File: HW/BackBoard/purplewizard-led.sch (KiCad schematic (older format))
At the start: 30 parts, among them U6 IS31FL3736

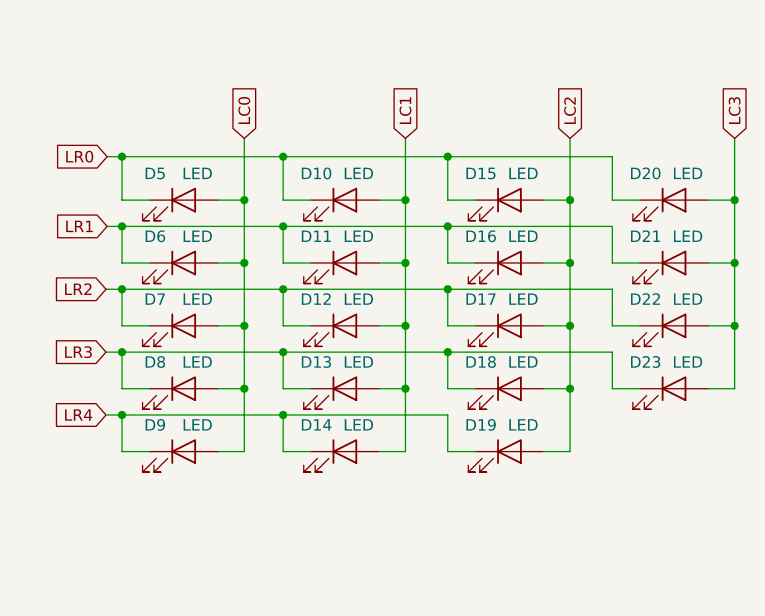
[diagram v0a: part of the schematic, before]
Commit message: Backboard - Move LCD connector over .3mm for better fitment of ribbon - Fix audio chip missing exposed pad bond to ground - Remove nRESET signal from JTAG - Reuse freed pin above to run an interrupt line from the keyboard controller to the MCU to enable interrupt driven keyboard input.  Protos will have a hack-n-jump to be feature compatible - Enlarge mounting holes from 3mm to 3.2mm to allow for slightly sloppier fitments - Move traces and vias a little further away from top mounting holes as they are now being used for standoffs instead of just lanyard holes - Move vias from pads of ghosting diodes off to the side to prevent excess solder wicking - Modify UPDI programming pads to include vias for easier connection of programmer - Enlarged fiducials - Moved LCD CS from high to low - Added more breakout pads for the LCD on the back - Swapped to a PAM2305 voltage regulator - Hardwired the LCD LED to ground - Added some breakout for a couple of processor GPIO - Moved silk for speaker placement down a little - Added logo for PCBX Artboard - Remove mask over eyes
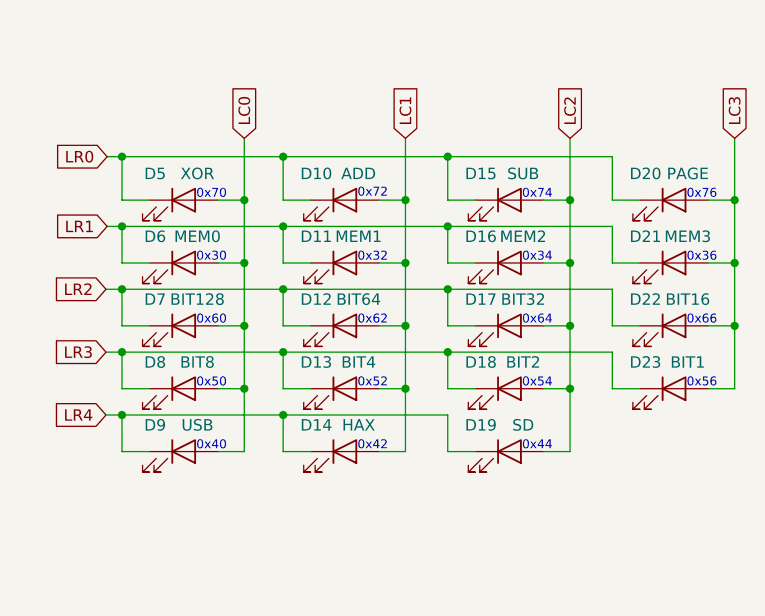
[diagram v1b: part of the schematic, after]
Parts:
- D10: value LED -> ADD
- D11: value LED -> MEM1
- D12: value LED -> BIT64
- D13: value LED -> BIT4
- D14: value LED -> HAX
- D15: value LED -> SUB
- D16: value LED -> MEM2
- D17: value LED -> BIT32
- D18: value LED -> BIT2
- D19: value LED -> SD
- D20: value LED -> PAGE
- D21: value LED -> MEM3
- D22: value LED -> BIT16
- D23: value LED -> BIT1
- D5: value LED -> XOR
- D6: value LED -> MEM0
- D7: value LED -> BIT128
- D8: value LED -> BIT8
- D9: value LED -> USB
- U6: footprint Package_DFN_QFN:QFN-40-1EP_5x5mm_P0.4mm_EP3.6x3.6mm_ThermalVias -> lib_fp:QFN-40-1EP_5x5mm_P0.4mm_EP3.6x3.6mm_LargerThermalVias
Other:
- note added: "0x30"
- note added: "0x32"
- note added: "0x34"
- note added: "0x36"
- note added: "0x40"
- note added: "0x42"
- note added: "0x44"
- note added: "0x50"
- note added: "0x52"
- note added: "0x54"
- note added: "0x56"
- note added: "0x60"
- note added: "0x62"
- note added: "0x64"
- note added: "0x66"
- note added: "0x70"
- note added: "0x72"
- note added: "0x74"
- note added: "0x76"
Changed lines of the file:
@@
 P 8620 3555
 F 0 "D10" H 8495 3670 50  0000 C CNN
-F 1 "LED" H 8680 3670 50  0000 C CNN
+F 1 "ADD" H 8680 3670 50  0000 C CNN
 F 2 "LED_SMD:LED_0603_1608Metric" H 8620 3555 50  0001 C CNN
 F 3 "~" H 8620 3555 50  0001 C CNN
@@
 P 8620 3830
 F 0 "D11" H 8495 3945 50  0000 C CNN
-F 1 "LED" H 8680 3945 50  0000 C CNN
+F 1 "MEM1" H 8680 3945 50  0000 C CNN
 F 2 "LED_SMD:LED_0603_1608Metric" H 8620 3830 50  0001 C CNN
 F 3 "~" H 8620 3830 50  0001 C CNN
@@
 P 8620 4105
 F 0 "D12" H 8495 4220 50  0000 C CNN
-F 1 "LED" H 8680 4220 50  0000 C CNN
+F 1 "BIT64" H 8680 4220 50  0000 C CNN
 F 2 "LED_SMD:LED_0603_1608Metric" H 8620 4105 50  0001 C CNN
 F 3 "~" H 8620 4105 50  0001 C CNN
@@
 P 8620 4380
 F 0 "D13" H 8495 4495 50  0000 C CNN
-F 1 "LED" H 8680 4495 50  0000 C CNN
+F 1 "BIT4" H 8680 4495 50  0000 C CNN
 F 2 "LED_SMD:LED_0603_1608Metric" H 8620 4380 50  0001 C CNN
 F 3 "~" H 8620 4380 50  0001 C CNN
@@
 P 8620 4655
 F 0 "D14" H 8495 4770 50  0000 C CNN
-F 1 "LED" H 8680 4770 50  0000 C CNN
+F 1 "HAX" H 8680 4770 50  0000 C CNN
 F 2 "LED_SMD:LED_0603_1608Metric" H 8620 4655 50  0001 C CNN
 F 3 "~" H 8620 4655 50  0001 C CNN
@@
 P 9340 3555
 F 0 "D15" H 9215 3670 50  0000 C CNN
-F 1 "LED" H 9400 3670 50  0000 C CNN
+F 1 "SUB" H 9400 3670 50  0000 C CNN
 F 2 "LED_SMD:LED_0603_1608Metric" H 9340 3555 50  0001 C CNN
 F 3 "~" H 9340 3555 50  0001 C CNN
@@
 P 9340 3830
 F 0 "D16" H 9215 3945 50  0000 C CNN
-F 1 "LED" H 9400 3945 50  0000 C CNN
+F 1 "MEM2" H 9400 3945 50  0000 C CNN
 F 2 "LED_SMD:LED_0603_1608Metric" H 9340 3830 50  0001 C CNN
 F 3 "~" H 9340 3830 50  0001 C CNN
@@
 P 9340 4105
 F 0 "D17" H 9215 4220 50  0000 C CNN
-F 1 "LED" H 9400 4220 50  0000 C CNN
+F 1 "BIT32" H 9400 4220 50  0000 C CNN
 F 2 "LED_SMD:LED_0603_1608Metric" H 9340 4105 50  0001 C CNN
 F 3 "~" H 9340 4105 50  0001 C CNN
@@
 P 9340 4380
 F 0 "D18" H 9215 4495 50  0000 C CNN
-F 1 "LED" H 9400 4495 50  0000 C CNN
+F 1 "BIT2" H 9400 4495 50  0000 C CNN
 F 2 "LED_SMD:LED_0603_1608Metric" H 9340 4380 50  0001 C CNN
 F 3 "~" H 9340 4380 50  0001 C CNN
@@
 P 9340 4655
 F 0 "D19" H 9215 4770 50  0000 C CNN
-F 1 "LED" H 9400 4770 50  0000 C CNN
+F 1 "SD" H 9400 4770 50  0000 C CNN
 F 2 "LED_SMD:LED_0603_1608Metric" H 9340 4655 50  0001 C CNN
 F 3 "~" H 9340 4655 50  0001 C CNN
@@
 P 10060 3555
 F 0 "D20" H 9935 3670 50  0000 C CNN
-F 1 "LED" H 10120 3670 50  0000 C CNN
+F 1 "PAGE" H 10120 3670 50  0000 C CNN
 F 2 "LED_SMD:LED_0603_1608Metric" H 10060 3555 50  0001 C CNN
 F 3 "~" H 10060 3555 50  0001 C CNN
@@
 P 10060 3830
 F 0 "D21" H 9935 3945 50  0000 C CNN
-F 1 "LED" H 10120 3945 50  0000 C CNN
+F 1 "MEM3" H 10120 3945 50  0000 C CNN
 F 2 "LED_SMD:LED_0603_1608Metric" H 10060 3830 50  0001 C CNN
 F 3 "~" H 10060 3830 50  0001 C CNN
@@
 P 10060 4105
 F 0 "D22" H 9935 4220 50  0000 C CNN
-F 1 "LED" H 10120 4220 50  0000 C CNN
+F 1 "BIT16" H 10120 4220 50  0000 C CNN
 F 2 "LED_SMD:LED_0603_1608Metric" H 10060 4105 50  0001 C CNN
 F 3 "~" H 10060 4105 50  0001 C CNN
@@
 P 10060 4380
 F 0 "D23" H 9935 4495 50  0000 C CNN
-F 1 "LED" H 10120 4495 50  0000 C CNN
+F 1 "BIT1" H 10120 4495 50  0000 C CNN
 F 2 "LED_SMD:LED_0603_1608Metric" H 10060 4380 50  0001 C CNN
 F 3 "~" H 10060 4380 50  0001 C CNN
@@
 P 7915 4655
 F 0 "D9" H 7790 4770 50  0000 C CNN
-F 1 "LED" H 7975 4770 50  0000 C CNN
+F 1 "USB" H 7975 4770 50  0000 C CNN
 F 2 "LED_SMD:LED_0603_1608Metric" H 7915 4655 50  0001 C CNN
 F 3 "~" H 7915 4655 50  0001 C CNN
@@
 P 7915 4380
 F 0 "D8" H 7790 4495 50  0000 C CNN
-F 1 "LED" H 7975 4495 50  0000 C CNN
+F 1 "BIT8" H 7975 4495 50  0000 C CNN
 F 2 "LED_SMD:LED_0603_1608Metric" H 7915 4380 50  0001 C CNN
 F 3 "~" H 7915 4380 50  0001 C CNN
@@
 P 7915 4105
 F 0 "D7" H 7790 4220 50  0000 C CNN
-F 1 "LED" H 7975 4220 50  0000 C CNN
+F 1 "BIT128" H 7975 4220 50  0000 C CNN
 F 2 "LED_SMD:LED_0603_1608Metric" H 7915 4105 50  0001 C CNN
 F 3 "~" H 7915 4105 50  0001 C CNN
@@
 P 7915 3830
 F 0 "D6" H 7790 3945 50  0000 C CNN
-F 1 "LED" H 7975 3945 50  0000 C CNN
+F 1 "MEM0" H 7975 3945 50  0000 C CNN
 F 2 "LED_SMD:LED_0603_1608Metric" H 7915 3830 50  0001 C CNN
 F 3 "~" H 7915 3830 50  0001 C CNN
@@
 P 7915 3555
 F 0 "D5" H 7790 3670 50  0000 C CNN
-F 1 "LED" H 7975 3670 50  0000 C CNN
+F 1 "XOR" H 7975 3670 50  0000 C CNN
 F 2 "LED_SMD:LED_0603_1608Metric" H 7915 3555 50  0001 C CNN
 F 3 "~" H 7915 3555 50  0001 C CNN
@@
 F 0 "U6" H 5765 5037 60  0000 C CNN
 F 1 "IS31FL3736" H 5765 4931 60  0000 C CNN
-F 2 "Package_DFN_QFN:QFN-40-1EP_5x5mm_P0.4mm_EP3.6x3.6mm_ThermalVias" H 5765 3940 60  0001 C CNN
+F 2 "lib_fp:QFN-40-1EP_5x5mm_P0.4mm_EP3.6x3.6mm_LargerThermalVias" H 5765 3940 60  0001 C CNN
 F 3 "" H 5765 3940 60  0001 C CNN
 	1    5765 3840
@@
 NoConn ~ 6365 4690
 NoConn ~ 6365 4790
+Text Notes 7970 3555 0    39   ~ 0
+0x70
+Text Notes 7970 3830 0    39   ~ 0
+0x30
+Text Notes 10115 3555 0    39   ~ 0
+0x76
+Text Notes 7970 4105 0    39   ~ 0
+0x60
+Text Notes 7970 4380 0    39   ~ 0
+0x50
+Text Notes 7970 4655 0    39   ~ 0
+0x40
+Text Notes 8675 3830 0    39   ~ 0
+0x32
+Text Notes 8675 3550 0    39   ~ 0
+0x72
+Text Notes 8675 4105 0    39   ~ 0
+0x62
+Text Notes 8675 4380 0    39   ~ 0
+0x52
+Text Notes 8675 4655 0    39   ~ 0
+0x42
+Text Notes 9395 4655 0    39   ~ 0
+0x44
+Text Notes 9395 3555 0    39   ~ 0
+0x74
+Text Notes 9395 3830 0    39   ~ 0
+0x34
+Text Notes 9395 4105 0    39   ~ 0
+0x64
+Text Notes 9395 4380 0    39   ~ 0
+0x54
+Text Notes 10115 4380 0    39   ~ 0
+0x56
+Text Notes 10115 4105 0    39   ~ 0
+0x66
+Text Notes 10115 3830 0    39   ~ 0
+0x36
 $EndSCHEMATC
